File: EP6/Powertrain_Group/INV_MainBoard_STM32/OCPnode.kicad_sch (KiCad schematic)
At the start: 11 parts, among them U19 LMV7219M5, U20 LMV7219M5

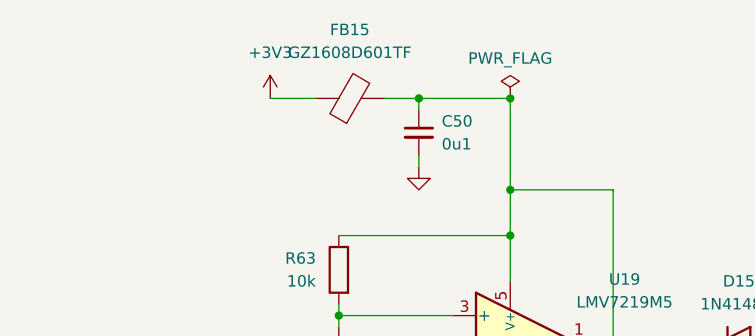
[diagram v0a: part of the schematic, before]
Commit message: batch update for JLCPCB 241117
6SBMS
ACC_HVLV1
INV_CurrentSense2
INV_CurrentSense3
DClinkCap1
INV_MainBoard_STM32
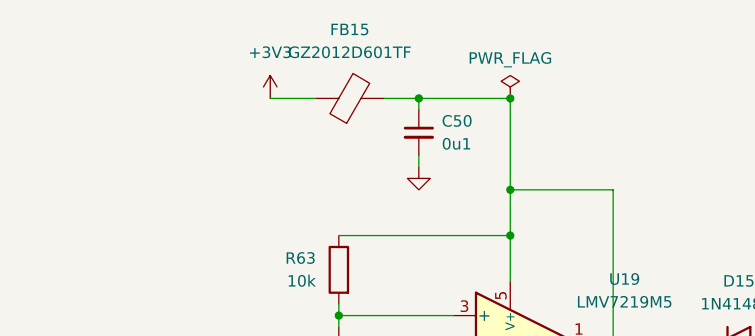
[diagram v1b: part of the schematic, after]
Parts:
- D15, D16: footprint Diode_SMD:D_SOD-123 -> Diode_SMD:D_SOD-323
- FB15: value GZ1608D601TF -> GZ2012D601TF
- R64, R65: footprint Resistor_SMD:R_0402_1005Metric -> Resistor_SMD:R_0603_1608Metric
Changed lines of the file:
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@@
 	(title_block
 		(title "INV_MainBoard")
-		(date "2024-11-15")
-		(rev "1")
+		(date "2024-11-16")
+		(rev "1.0")
 		(company "NTURacing Team")
 		(comment 1 "郭哲明 Jack Kuo")
@@
 			)
 		)
-		(property "Footprint" "Diode_SMD:D_SOD-123"
+		(property "Footprint" "Diode_SMD:D_SOD-323"
 			(at 144.78 130.175 0)
 			(effects
@@
 			)
 		)
-		(property "Footprint" "Diode_SMD:D_SOD-123"
+		(property "Footprint" "Diode_SMD:D_SOD-323"
 			(at 148.59 75.565 0)
 			(effects
@@
 			)
 		)
-		(property "Value" "GZ1608D601TF"
+		(property "Value" "GZ2012D601TF"
 			(at 105.3592 39.37 90)
 			(effects
@@
 			)
 		)
-		(property "Footprint" "Resistor_SMD:R_0402_1005Metric"
+		(property "Footprint" "Resistor_SMD:R_0603_1608Metric"
 			(at 104.648 123.19 90)
 			(effects
@@
 			)
 		)
-		(property "Footprint" "Resistor_SMD:R_0402_1005Metric"
+		(property "Footprint" "Resistor_SMD:R_0603_1608Metric"
 			(at 105.918 73.66 90)
 			(effects

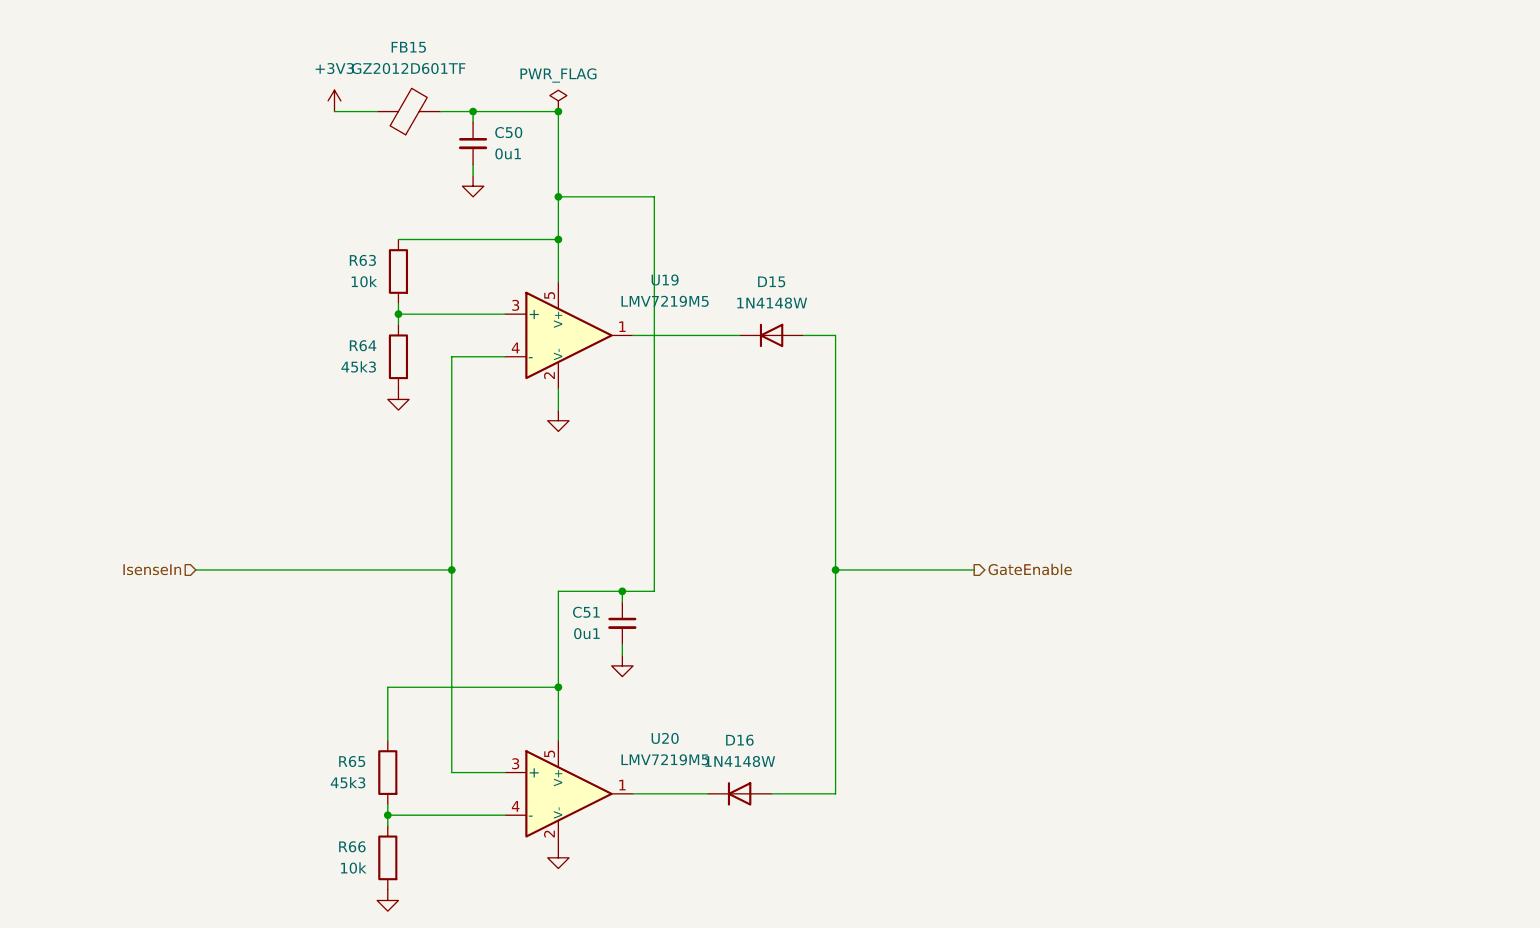
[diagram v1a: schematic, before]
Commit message: update INV_MainBoard_STM32 to V2.0
big update to match new INV_GateDriver
and use H743ZI as MCU
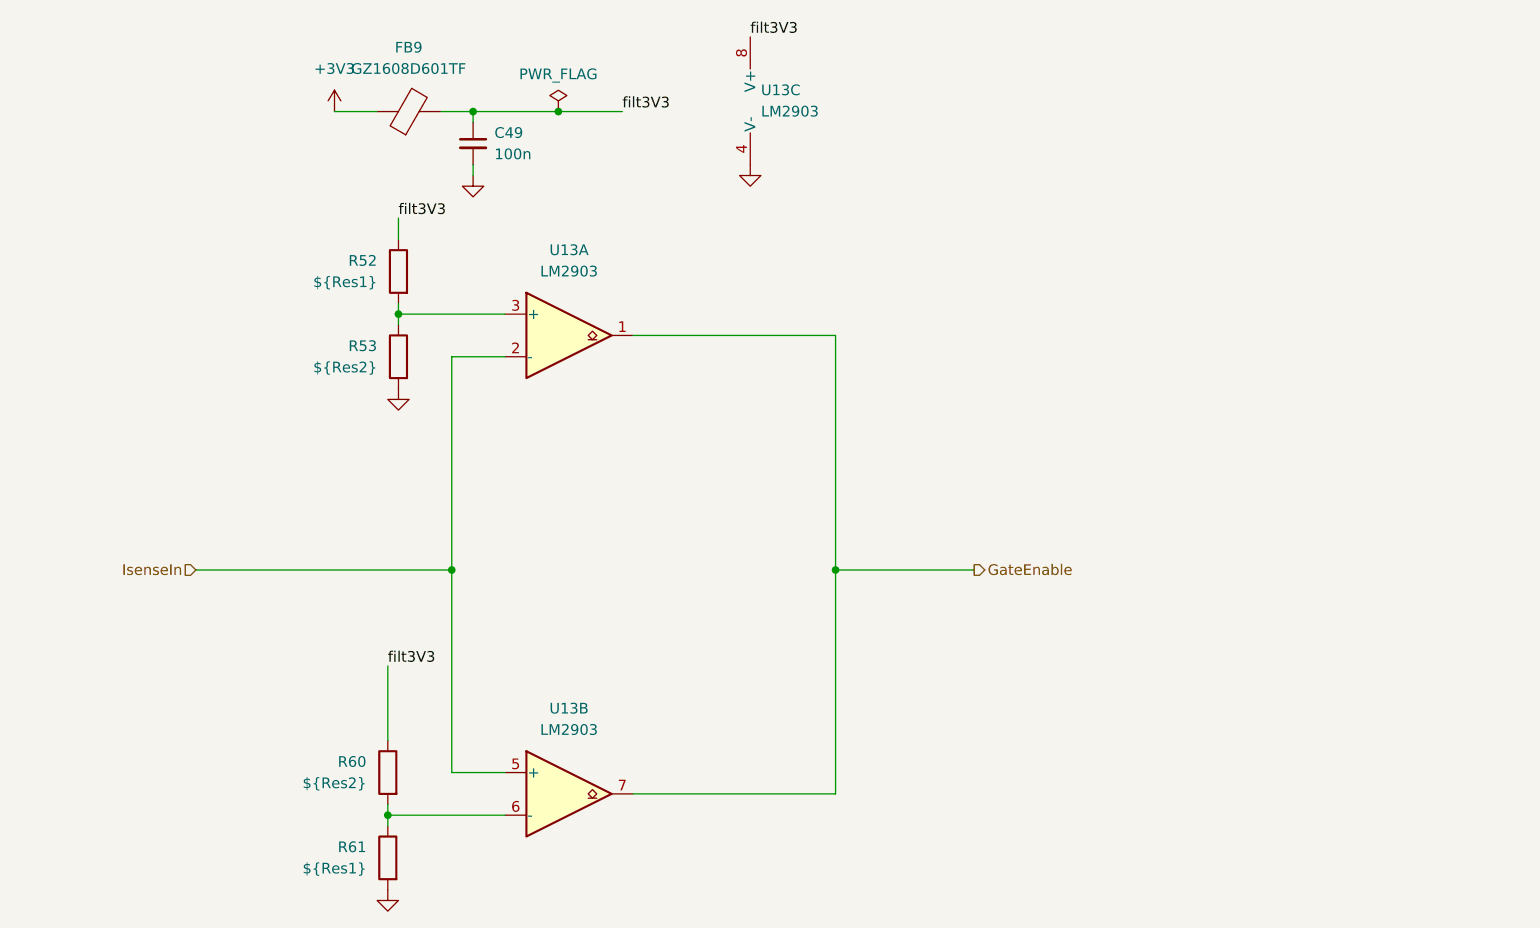
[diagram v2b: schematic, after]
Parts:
- removed C50, C51: 0u1, Capacitor_SMD:C_0402_1005Metric, symbol Device:C_Small
- removed D15, D16: 1N4148W, Diode_SMD:D_SOD-323, symbol Diode:1N4148W
- removed FB15: GZ2012D601TF, Inductor_SMD:L_0805_2012Metric, symbol Device:FerriteBead
- removed R63, R66: 10k, Resistor_SMD:R_0402_1005Metric, symbol Device:R
- removed R64, R65: 45k3, Resistor_SMD:R_0603_1608Metric, symbol Device:R
- removed U19, U20: LMV7219M5, PCM_Package_TO_SOT_SMD_AKL:SOT-23-5, symbol PCM_Analog_Comparator_AKL:LMV7219M5
- added C49: 100n, Capacitor_SMD:C_0402_1005Metric, symbol Device:C_Small
- added FB9: GZ1608D601TF, Capacitor_SMD:C_0603_1608Metric, symbol Device:FerriteBead
- added R52, R61: ${Res1}, Resistor_SMD:R_0402_1005Metric, symbol Device:R
- added R53, R60: ${Res2}, Resistor_SMD:R_0402_1005Metric, symbol Device:R
- added U13: LM2903, Package_SO:SOIC-8_3.9x4.9mm_P1.27mm, symbol Comparator:LM2903
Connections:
- net +3V3: now also FB9.1
- net GND: now also C49.2, R53.2, R61.2, U13.4 (V-)
- net GateEnable: now also U13.1, U13.7
- net IsenseIn: now also U13.2 (-), U13.5 (+)
- new net: R60.2, R61.1, U13.6 (-)
- new net: R52.2, R53.1, U13.3 (+)
- new net filt3V3: C49.1, FB9.2, R52.1, R60.1, U13.8 (V+)
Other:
- title: INV_MainBoard -> INV_MainBoard_STM32

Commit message: update INV_MainBoard_STM32 to V2.1
update for JLCPCB, include change in 1.65 Vref and some name change for easier JLCPCBA BOM selection
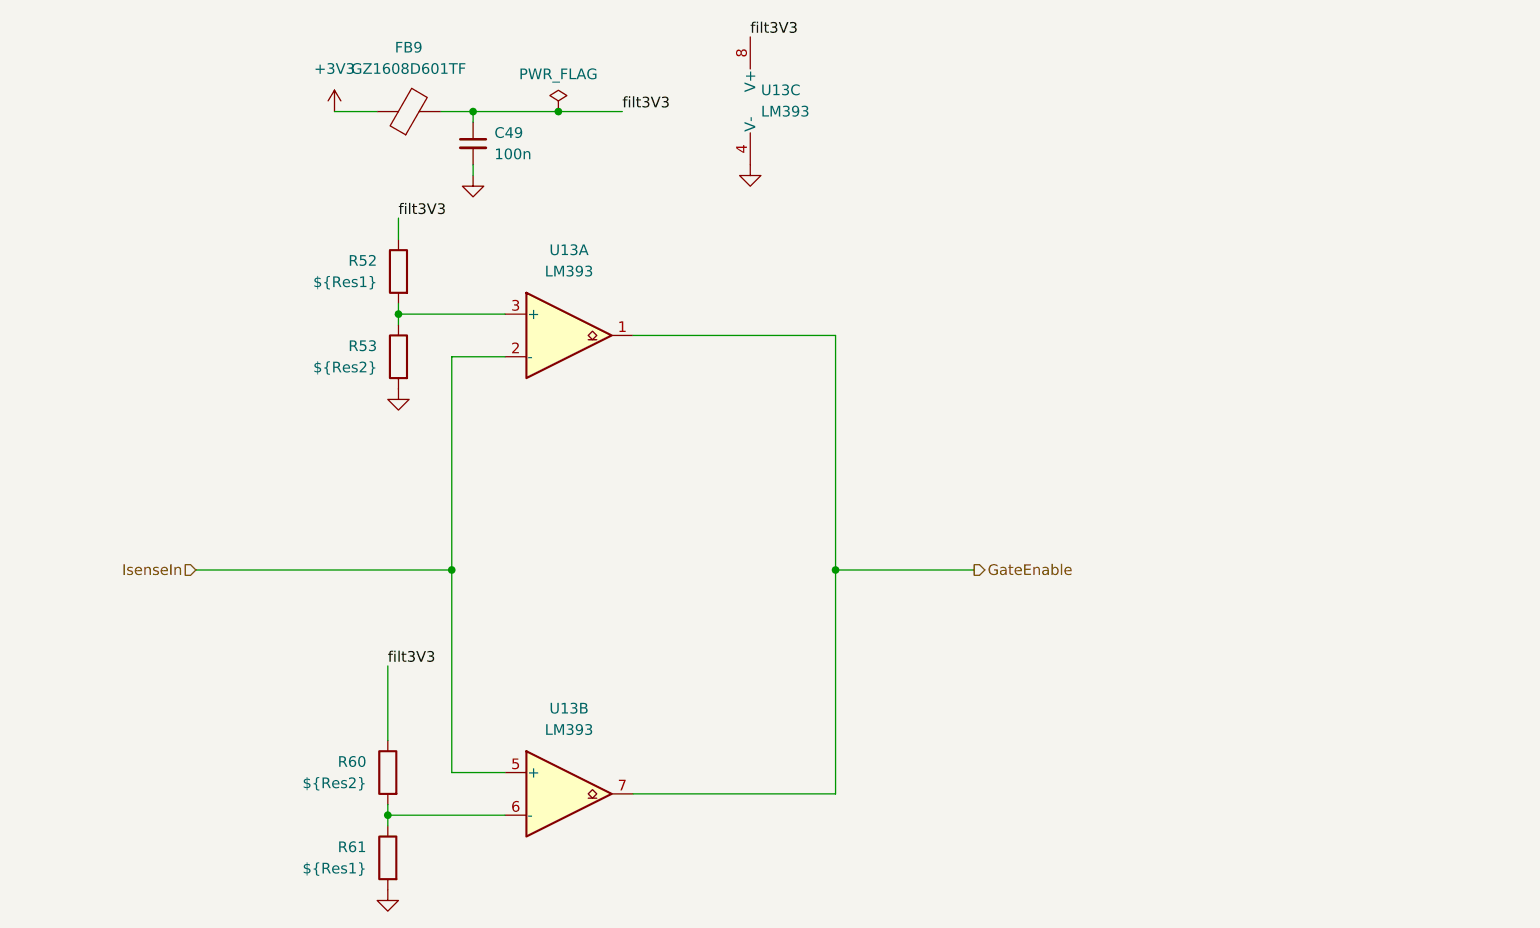
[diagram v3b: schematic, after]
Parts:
- U13: value LM2903 -> LM393; symbol Comparator:LM2903 -> Comparator:LM393
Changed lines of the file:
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@@
 	(title_block
 		(title "INV_MainBoard_STM32")
-		(rev "2.0")
+		(date "2025-02-28")
+		(rev "2.1")
 		(company "NTURacing Team")
 		(comment 1 "郭哲明 Jack Kuo")
@@
 	)
 	(symbol
-		(lib_id "Comparator:LM2903")
+		(lib_id "Comparator:LM393")
 		(at 148.59 43.18 0)
 		(unit 3)
@@
 			)
 		)
-		(property "Value" "LM2903"
+		(property "Value" "LM393"
 			(at 147.32 44.45 0)
 			(effects
@@
 			)
 		)
-		(property "Description" "Low-Power, Low-Offset Voltage, Dual Comparators, DIP-8/SOIC-8/SOP-8/TSSOP-8/VSSOP-8"
+		(property "Description" "Low-Power, Low-Offset Voltage, Dual Comparators, DIP-8/SOIC-8/TO-99-8"
 			(at 148.59 43.18 0)
 			(effects
@@
 	)
 	(symbol
-		(lib_id "Comparator:LM2903")
+		(lib_id "Comparator:LM393")
 		(at 124.46 71.12 0)
 		(unit 1)
@@
 			)
 		)
-		(property "Value" "LM2903"
+		(property "Value" "LM393"
 			(at 124.46 63.5 0)
 			(effects
@@
 			)
 		)
-		(property "Description" "Low-Power, Low-Offset Voltage, Dual Comparators, DIP-8/SOIC-8/SOP-8/TSSOP-8/VSSOP-8"
+		(property "Description" "Low-Power, Low-Offset Voltage, Dual Comparators, DIP-8/SOIC-8/TO-99-8"
 			(at 124.46 71.12 0)
 			(effects
@@
 	)
 	(symbol
-		(lib_id "Comparator:LM2903")
+		(lib_id "Comparator:LM393")
 		(at 124.46 125.73 0)
 		(unit 2)
@@
 			)
 		)
-		(property "Value" "LM2903"
+		(property "Value" "LM393"
 			(at 124.46 118.11 0)
 			(effects
@@
 			)
 		)
-		(property "Description" "Low-Power, Low-Offset Voltage, Dual Comparators, DIP-8/SOIC-8/SOP-8/TSSOP-8/VSSOP-8"
+		(property "Description" "Low-Power, Low-Offset Voltage, Dual Comparators, DIP-8/SOIC-8/TO-99-8"
 			(at 124.46 125.73 0)
 			(effects
